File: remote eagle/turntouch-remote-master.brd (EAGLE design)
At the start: 36.8 x 36.8 mm, 17 parts, among them J1 TC2030-JLINK-NL, Q1 CRYSTAL.ABS07, U1 MDBT40SMD

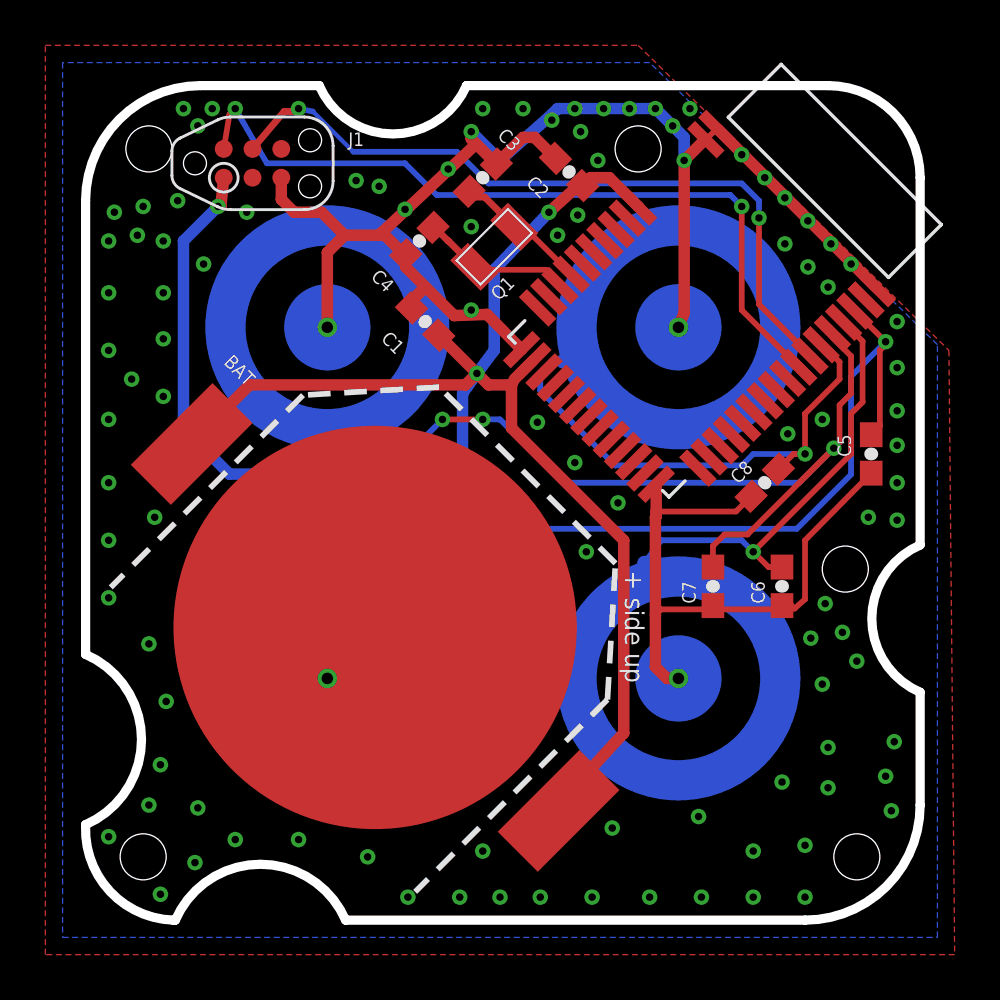
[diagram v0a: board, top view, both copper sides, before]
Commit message: Rev 37. Moving a single mounting peg. Also rearranging a few ground vias.
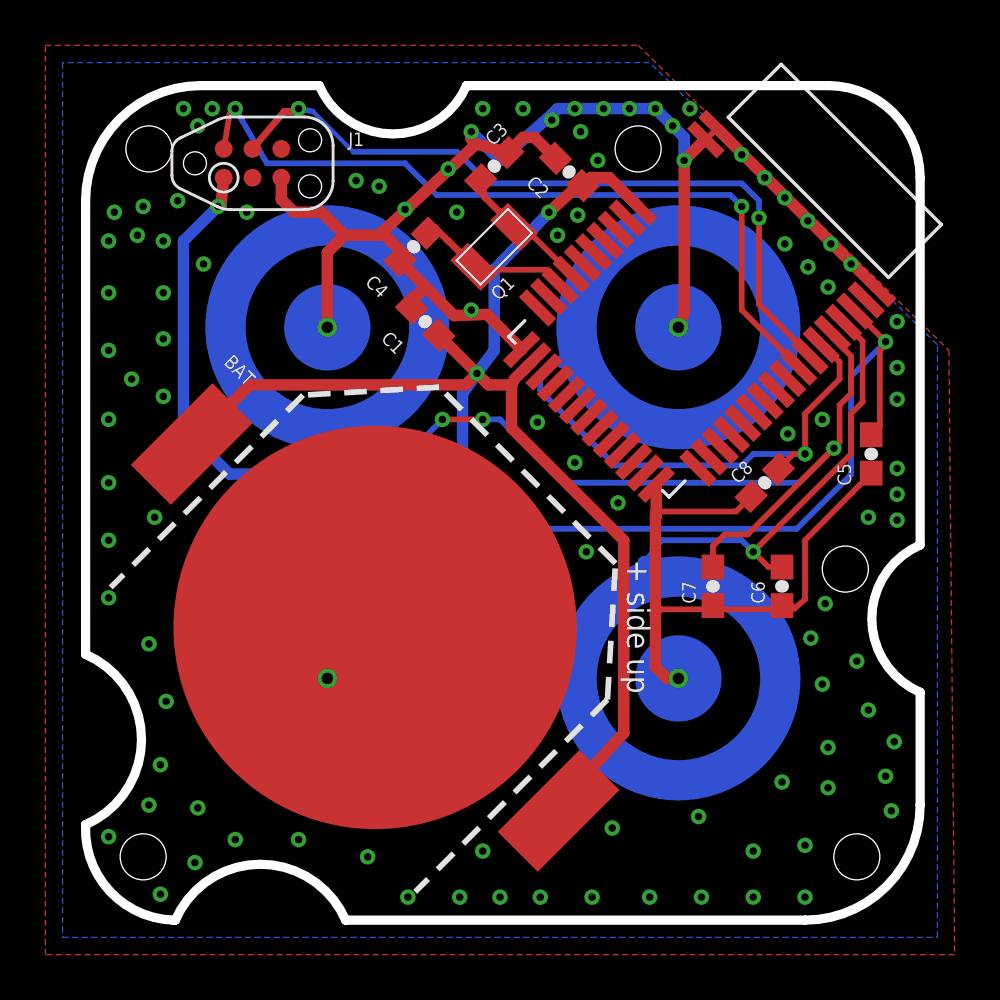
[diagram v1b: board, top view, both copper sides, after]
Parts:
- moved C3 0.72 mm to (18.0, 33.3)
- moved C4 0.36 mm to (14.5, 29.7)
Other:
- board text added: "Mar 28 2017"
- board text removed: "Mar 20 2017"
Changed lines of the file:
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@@
 <plain>
 <text x="26.162" y="17.78" size="0.8382" layer="26" font="vector" ratio="9" rot="SMR0" align="top-center">Rev. 37</text>
-<text x="9.398" y="20.574" size="1.27" layer="26" font="vector" ratio="9" rot="SMR0" align="top-center">TURN TOUCH</text>
+<text x="9.398" y="20.32" size="1.27" layer="26" font="vector" ratio="9" rot="SMR0" align="top-center">TURN TOUCH</text>
 <hole x="2.794" y="34.036" drill="2.032"/>
 <hole x="34.036" y="2.794" drill="2.032"/>
@@
 <wire x1="34.544" y1="34.544" x2="34.544" y2="31.496" width="1.016" layer="22"/>
 <hole x="33.528" y="15.494" drill="2.032"/>
-<text x="26.162" y="20.066" size="0.8382" layer="26" font="vector" ratio="9" rot="SMR0" align="top-center">Mar 20 2017</text>
-<text x="24.638" y="12.954" size="0.8382" layer="25" font="vector" ratio="9" rot="SR270" align="top-center">+ side up</text>
+<text x="26.162" y="20.066" size="0.8382" layer="26" font="vector" ratio="9" rot="SMR0" align="top-center">Mar 28 2017</text>
+<text x="24.892" y="12.954" size="1" layer="25" font="vector" ratio="9" rot="SR270" align="top-center">+ side up</text>
 </plain>
 <attributes>
@@
 <attribute name="VALUE" x="19.382609375" y="22.211040625" size="0.6" layer="27" ratio="9" rot="R315"/>
 </element>
-<element name="C3" library="SparkFun-Capacitors" package="0603-CAP" value="12pF" x="17.526" y="32.766" smashed="yes" rot="R45">
-<attribute name="PROD_ID" value="CAP-00810" x="17.526" y="32.766" size="1.778" layer="27" rot="R45" display="off"/>
-<attribute name="NAME" x="19.257775" y="34.31443125" size="0.6" layer="25" font="vector" ratio="9" rot="R135"/>
-</element>
-<element name="C4" library="SparkFun-Capacitors" package="0603-CAP" value="12pF" x="14.732" y="29.972" smashed="yes" rot="R225">
-<attribute name="PROD_ID" value="CAP-00810" x="14.732" y="29.972" size="1.778" layer="27" rot="R225" display="off"/>
-<attribute name="NAME" x="13.6750625" y="28.08614375" size="0.6" layer="25" font="vector" ratio="9" rot="R135"/>
+<element name="C3" library="SparkFun-Capacitors" package="0603-CAP" value="12pF" x="18.034" y="33.274" smashed="yes" rot="R45">
+<attribute name="PROD_ID" value="CAP-00810" x="18.034" y="33.274" size="1.778" layer="27" rot="R45" display="off"/>
+<attribute name="NAME" x="18.26356875" y="35.259775" size="0.6" layer="25" font="vector" ratio="9" rot="R225"/>
+</element>
+<element name="C4" library="SparkFun-Capacitors" package="0603-CAP" value="12pF" x="14.478" y="29.718" smashed="yes" rot="R225">
+<attribute name="PROD_ID" value="CAP-00810" x="14.478" y="29.718" size="1.778" layer="27" rot="R225" display="off"/>
+<attribute name="NAME" x="13.4210625" y="27.83214375" size="0.6" layer="25" font="vector" ratio="9" rot="R135"/>
 </element>
 <element name="C2" library="SparkFun-Capacitors" package="0603-CAP" value="1uF" x="21.336" y="33.02" smashed="yes" rot="R135">
@@
 <element name="C5" library="SparkFun-Capacitors" package="0603-CAP" value="100nF" x="34.671" y="20.574" smashed="yes" rot="R90">
 <attribute name="PROD_ID" value="CAP-00810" x="34.671" y="20.574" size="1.778" layer="27" rot="R90" display="off"/>
-<attribute name="NAME" x="33.782" y="20.447" size="0.6" layer="25" font="vector" ratio="9" rot="R90"/>
+<attribute name="NAME" x="33.782" y="19.177" size="0.6" layer="25" font="vector" ratio="9" rot="R90"/>
 <attribute name="VALUE" x="35.814" y="19.558" size="0.6" layer="27" font="vector" ratio="9" rot="R90"/>
 </element>
@@
 <wire x1="17.018" y1="34.798" x2="17.018" y2="34.47608125" width="0.508" layer="1"/>
 <wire x1="17.018" y1="34.47608125" x2="17.238040625" y2="34.256040625" width="0.508" layer="1"/>
-<wire x1="17.238040625" y1="34.256040625" x2="18.127040625" y2="33.367040625" width="0.508" layer="1"/>
+<wire x1="17.238040625" y1="34.256040625" x2="18.635040625" y2="33.875040625" width="0.508" layer="1"/>
 <wire x1="20.646959375" y1="33.367040625" x2="20.646959375" y2="33.709040625" width="0.508" layer="1"/>
 <wire x1="20.646959375" y1="33.709040625" x2="19.812" y2="34.544" width="0.508" layer="1"/>
 <wire x1="19.812" y1="34.544" x2="19.304" y2="34.544" width="0.508" layer="1"/>
-<wire x1="19.304" y1="34.544" x2="18.127040625" y2="33.367040625" width="0.508" layer="1"/>
-<wire x1="14.13095625" y1="29.37095625" x2="14.06304375" y2="29.37095625" width="0.508" layer="1"/>
+<wire x1="19.304" y1="34.544" x2="18.635040625" y2="33.875040625" width="0.508" layer="1"/>
+<wire x1="13.87695625" y1="29.11695625" x2="14.06304375" y2="29.37095625" width="0.508" layer="1"/>
 <wire x1="17.238040625" y1="34.256040625" x2="13.081" y2="30.353" width="0.508" layer="1"/>
 <wire x1="13.081" y1="30.353" x2="12.954" y2="30.226" width="0.508" layer="1"/>
@@
 <wire x1="29.37095625" y1="18.70295625" x2="28.702" y2="18.034" width="0.254" layer="1"/>
 <wire x1="28.702" y1="18.034" x2="25.180884375" y2="18.034" width="0.254" layer="1"/>
-<wire x1="14.13095625" y1="29.37095625" x2="14.13095625" y2="28.813621875" width="0.508" layer="1"/>
+<wire x1="13.87695625" y1="29.11695625" x2="14.13095625" y2="28.813621875" width="0.508" layer="1"/>
 <wire x1="14.13095625" y1="28.813621875" x2="14.995290625" y2="27.9492875" width="0.508" layer="1"/>
 <wire x1="14.995290625" y1="27.9492875" x2="16.26495" y2="26.679628125" width="0.508" layer="1"/>
@@
 <via x="35.814" y="26.416" extent="1-16" drill="0.3302"/>
 <via x="35.814" y="24.384" extent="1-16" drill="0.3302"/>
-<via x="35.814" y="19.304" extent="1-16" drill="0.3302"/>
+<via x="35.814" y="18.796" extent="1-16" drill="0.3302"/>
 <via x="32.639" y="13.97" extent="1-16" drill="0.3302"/>
 <via x="35.687" y="7.874" extent="1-16" drill="0.3302"/>
@@
 <via x="35.814" y="17.653" extent="1-16" drill="0.3302"/>
 <via x="34.544" y="17.78" extent="1-16" drill="0.3302"/>
-<via x="33.401" y="12.7" extent="1-16" drill="0.3302"/>
+<via x="16.383" y="31.242" extent="1-16" drill="0.3302"/>
 <via x="32.004" y="12.446" extent="1-16" drill="0.3302"/>
 <via x="32.512" y="10.414" extent="1-16" drill="0.3302"/>
@@
 <via x="3.429" y="29.972" extent="1-16" drill="0.3302"/>
 <via x="3.429" y="27.686" extent="1-16" drill="0.3302"/>
-<via x="35.814" y="22.479" extent="1-16" drill="0.3302"/>
-<via x="35.814" y="20.955" extent="1-16" drill="0.3302"/>
+<via x="35.814" y="22.987" extent="1-16" drill="0.3302"/>
+<via x="35.814" y="19.939" extent="1-16" drill="0.3302"/>
 <via x="19.939" y="21.971" extent="1-16" drill="0.3302"/>
 <via x="23.495" y="18.415" extent="1-16" drill="0.3302"/>
 <via x="21.59" y="20.193" extent="1-16" drill="0.3302"/>
-<via x="17.018" y="30.607" extent="1-16" drill="0.3302"/>
+<via x="34.544" y="9.271" extent="1-16" drill="0.3302"/>
 <via x="21.717" y="31.115" extent="1-16" drill="0.3302"/>
 <via x="20.828" y="30.226" extent="1-16" drill="0.3302"/>
@@
 <wire x1="20.32" y1="28.702" x2="20.93824375" y2="28.08375625" width="0.254" layer="1"/>
 <wire x1="20.93824375" y1="28.08375625" x2="20.93824375" y2="28.0093125" width="0.254" layer="1"/>
-<wire x1="15.333040625" y1="30.573040625" x2="15.411190625" y2="30.573040625" width="0.254" layer="1"/>
+<wire x1="15.079040625" y1="30.319040625" x2="15.411190625" y2="30.573040625" width="0.254" layer="1"/>
 <contactref element="Q1" pad="2"/>
 <wire x1="15.411190625" y1="30.573040625" x2="15.411190625" y2="30.562809375" width="0.3048" layer="1"/>
@@
 <contactref element="U1" pad="9"/>
 <contactref element="C3" pad="1"/>
-<wire x1="17.17895625" y1="31.91095625" x2="16.92495625" y2="32.16495625" width="0.254" layer="1"/>
 <contactref element="Q1" pad="1"/>
-<wire x1="17.17895625" y1="31.91095625" x2="17.60880625" y2="31.91095625" width="0.3048" layer="1"/>
+<wire x1="17.43295625" y1="32.67295625" x2="17.60880625" y2="31.91095625" width="0.3048" layer="1"/>
 <wire x1="17.60880625" y1="31.91095625" x2="18.91788125" y2="30.60188125" width="0.3048" layer="1"/>
 <wire x1="18.91788125" y1="30.60188125" x2="19.335625" y2="30.60188125" width="0.254" layer="1"/>

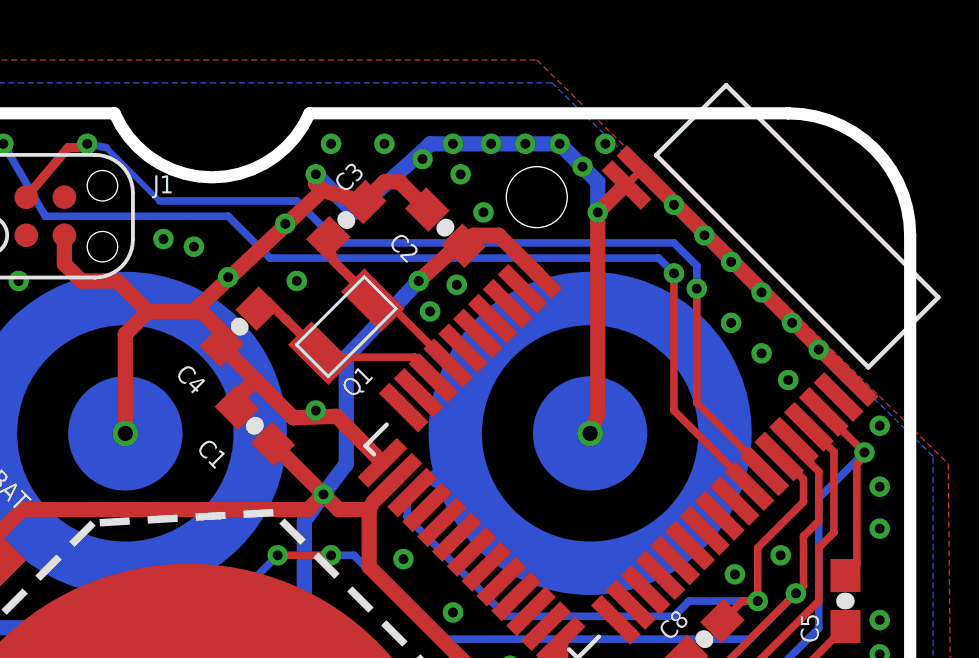
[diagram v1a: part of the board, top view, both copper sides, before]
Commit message: Revision 38. Just moving mounting pegs.
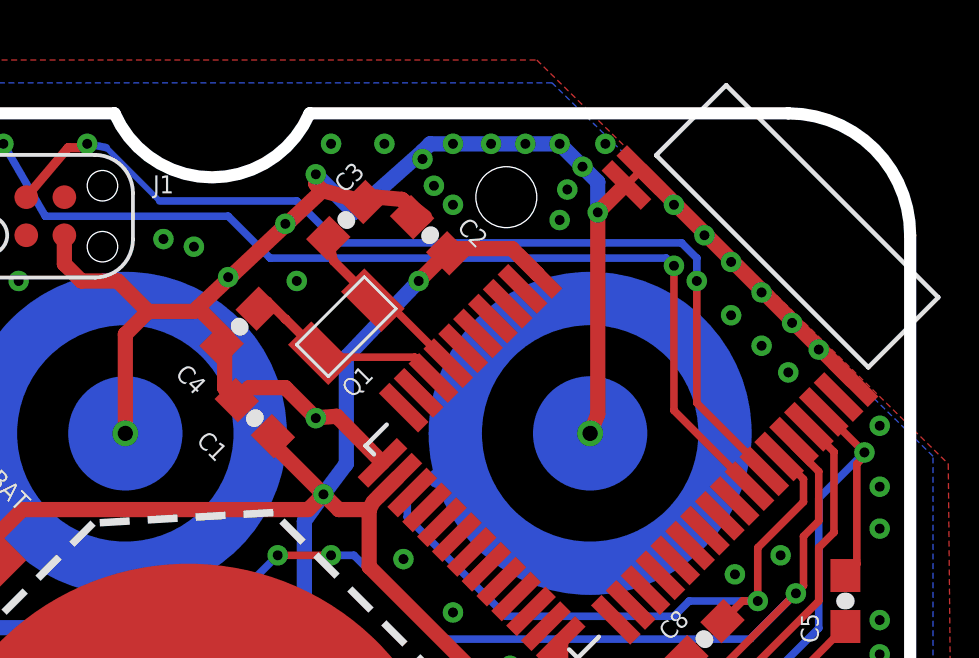
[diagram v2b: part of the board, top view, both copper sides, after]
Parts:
- moved C2 0.57 mm to (20.8, 32.8)
- moved C1 0.25 mm to (15.0, 26.7)
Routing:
- net GND: track 98.0 -> 97.4 mm
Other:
- board text added: "April 10 2017"
- board text added: "Rev. 38"
- board text removed: "Mar 28 2017"
- board text removed: "Rev. 37"
